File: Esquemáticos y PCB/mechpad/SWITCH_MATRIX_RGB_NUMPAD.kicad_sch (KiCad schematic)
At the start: 116 parts, among them SW100 NUMPAD17, SW101 NUMPAD18, SW102 NUMPAD19, SW103 NUMPAD20, SW84 NUMPAD1, SW85 NUMPAD2, SW86 NUMPAD3, SW87 NUMPAD4, SW88 NUMPAD5, SW89 NUMPAD6, SW90 NUMPAD7, SW91 NUMPAD8, SW92 NUMPAD9, SW93 NUMPAD10, SW94 NUMPAD11, SW95 NUMPAD12, SW96 NUMPAD13, SW97 NUMPAD14, SW98 NUMPAD15, SW99 NUMPAD16

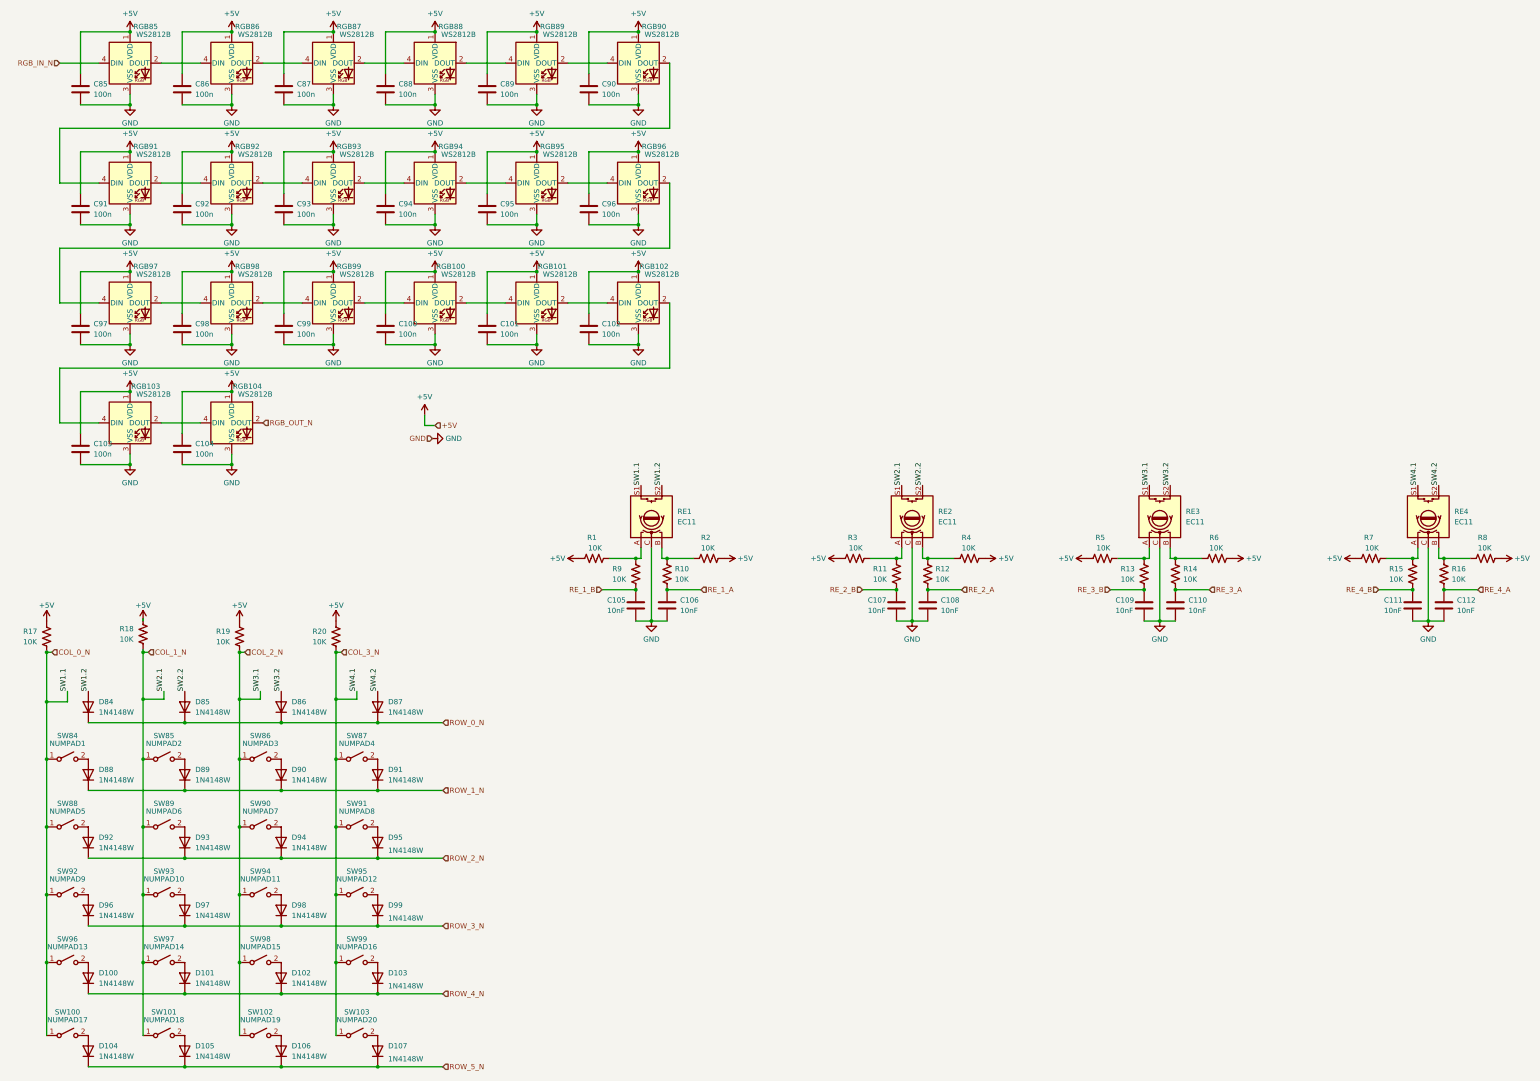
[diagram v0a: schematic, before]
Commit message: Updated schematic
Added connections between hierarchical sheets, more code testing
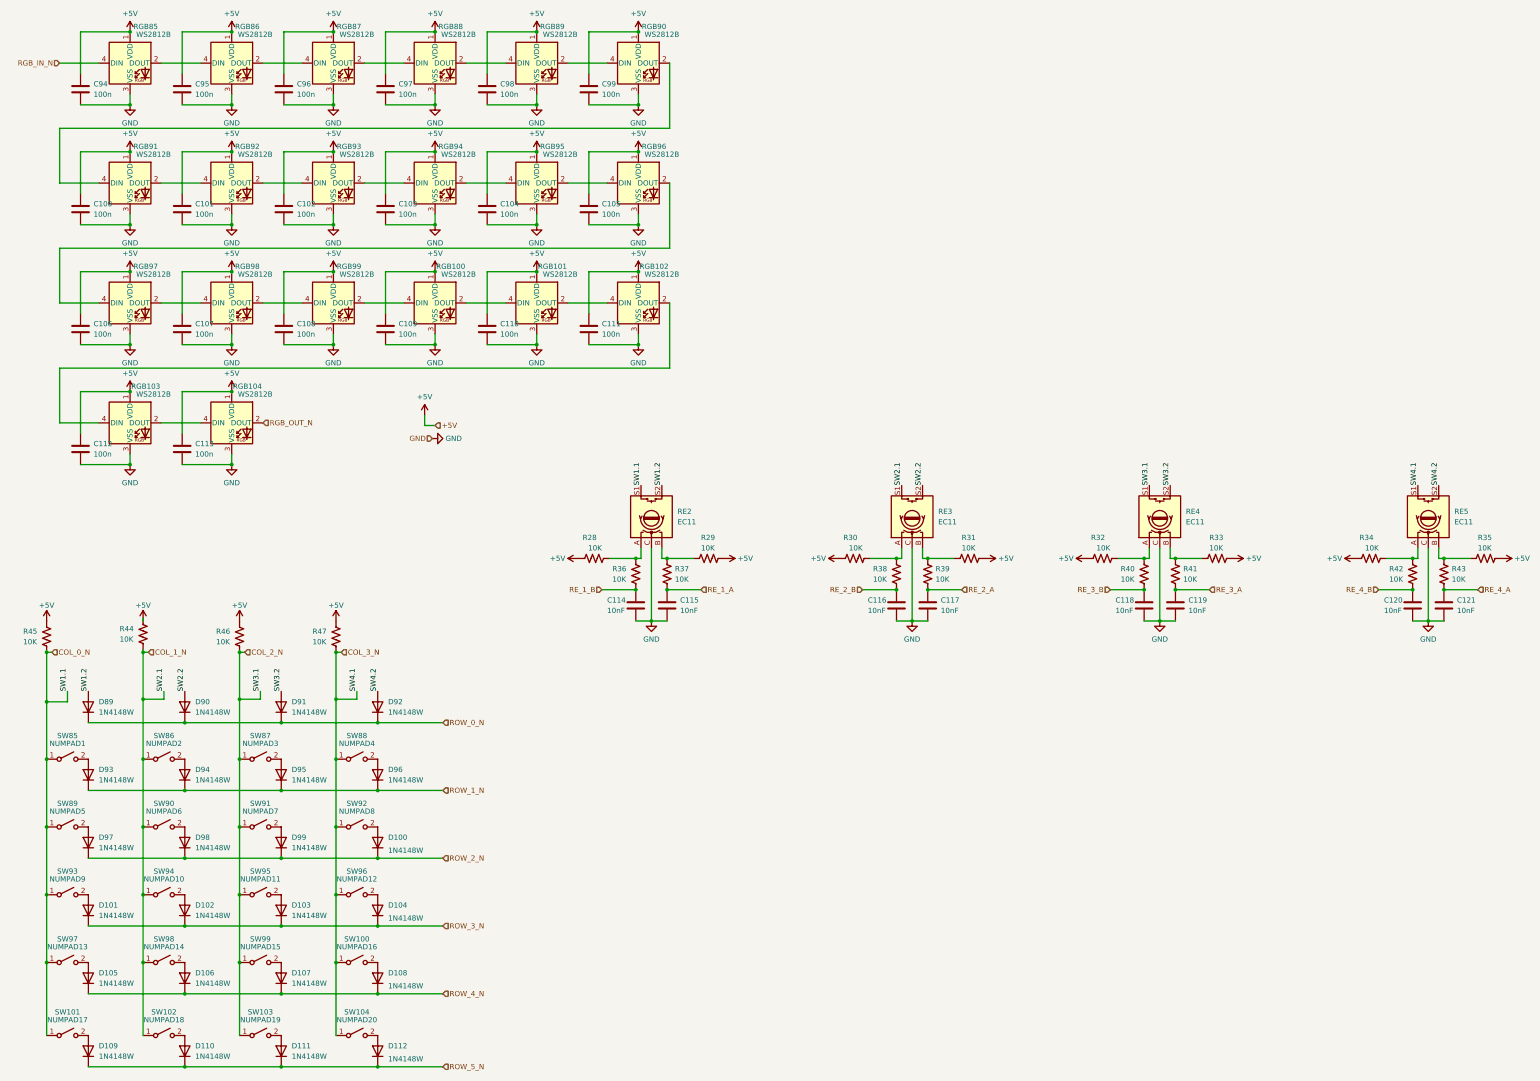
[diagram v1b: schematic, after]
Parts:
- renumbered C91 to C100, C92 to C101, C93 to C102, C94 to C103, C95 to C104, C96 to C105, C97 to C106, C98 to C107, C99 to C108, C100 to C109, C101 to C110, C102 to C111, C103 to C112, C104 to C113, C105 to C114, C106 to C115, C107 to C116, C108 to C117, C109 to C118, C110 to C119, C111 to C120, C112 to C121, C85 to C94, C86 to C95, C87 to C96, C88 to C97, C89 to C98, C90 to C99, D95 to D100, D96 to D101, D97 to D102, D98 to D103, D99 to D104, D100 to D105, D101 to D106, D102 to D107, D103 to D108, D104 to D109, D105 to D110, D106 to D111, D107 to D112, D84 to D89, D85 to D90, D86 to D91, D87 to D92, D88 to D93, D89 to D94, D90 to D95, D91 to D96, D92 to D97, D93 to D98, D94 to D99, R1 to R28, R2 to R29, R3 to R30, R4 to R31, R5 to R32, R6 to R33, R7 to R34, R8 to R35, R9 to R36, R10 to R37, R11 to R38, R12 to R39, R13 to R40, R14 to R41, R15 to R42, R16 to R43, R18 to R44, R17 to R45, R19 to R46, R20 to R47, RE1 to RE2, RE2 to RE3, RE3 to RE4, RE4 to RE5, SW99 to SW100, SW100 to SW101, SW101 to SW102, SW102 to SW103, SW103 to SW104, SW84 to SW85, SW85 to SW86, SW86 to SW87, SW87 to SW88, SW88 to SW89, SW89 to SW90, SW90 to SW91, SW91 to SW92, SW92 to SW93, SW93 to SW94, SW94 to SW95, SW95 to SW96, SW96 to SW97, SW97 to SW98, SW98 to SW99
